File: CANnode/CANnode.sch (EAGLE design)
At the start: 244 parts, among them IC1 ISO1050DUB, IC2 ISO1050DUB, Q1 FDV302P, Q3 FDV302P, U1 LM324PW, U10 FT2232HL, U11 93LC56C-I/SN, U2 TPS70445_PWP_24, U3 LM324PW, U4 LM324PW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

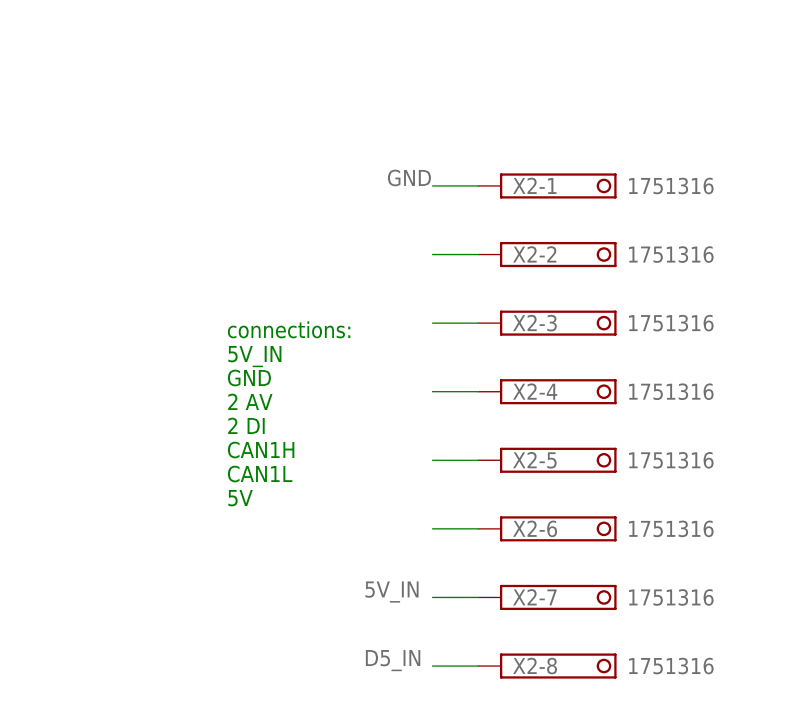
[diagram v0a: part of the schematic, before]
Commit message: Finished Debug headers
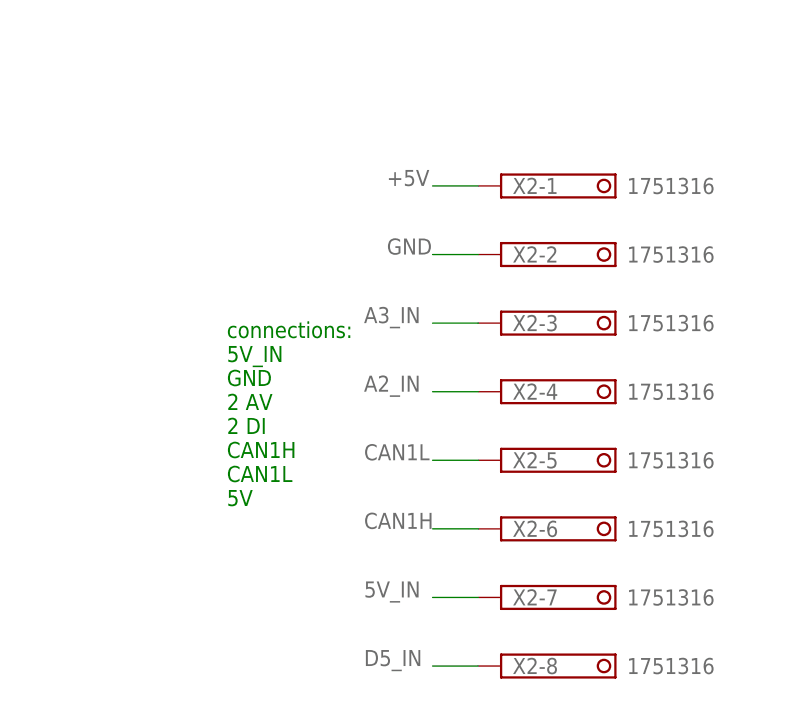
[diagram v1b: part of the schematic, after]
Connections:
- removed net N$44: X2-6.K
- removed net N$69: X2-5.K
- removed net N$70: X2-4.K
- removed net N$71: X2-3.K
- removed net N$72: X2-2.K
- net +5V: now also X2-1.K
- net A2_IN: now also X2-4.K
- net A3_IN: now also X2-3.K
- net CAN1H: now also X2-6.K
- net CAN1L: now also X2-5.K
- net GND: now also X2-2.K; no longer X2-1.K
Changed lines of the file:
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@@
 <label x="233.68" y="-160.02" size="1.778" layer="95"/>
 </segment>
+<segment>
+<pinref part="X2" gate="-6" pin="K"/>
+<wire x1="180.34" y1="-175.26" x2="175.26" y2="-175.26" width="0.1524" layer="91"/>
+<label x="167.64" y="-175.26" size="1.778" layer="95"/>
+</segment>
 </net>
 <net name="CAN1L" class="0">
@@
 <label x="233.68" y="-162.56" size="1.778" layer="95"/>
 </segment>
+<segment>
+<pinref part="X2" gate="-5" pin="K"/>
+<wire x1="180.34" y1="-167.64" x2="175.26" y2="-167.64" width="0.1524" layer="91"/>
+<label x="167.64" y="-167.64" size="1.778" layer="95"/>
+</segment>
 </net>
 <net name="CAN2L" class="0">
@@
 </segment>
 <segment>
-<pinref part="X2" gate="-1" pin="K"/>
-<wire x1="180.34" y1="-137.16" x2="175.26" y2="-137.16" width="0.1524" layer="91"/>
-<label x="170.18" y="-137.16" size="1.778" layer="95"/>
+<pinref part="X2" gate="-2" pin="K"/>
+<wire x1="180.34" y1="-144.78" x2="175.26" y2="-144.78" width="0.1524" layer="91"/>
+<label x="170.18" y="-144.78" size="1.778" layer="95"/>
 </segment>
 </net>
@@
 <wire x1="502.92" y1="-40.64" x2="505.46" y2="-40.64" width="0.1524" layer="91"/>
 </segment>
+<segment>
+<pinref part="X2" gate="-1" pin="K"/>
+<wire x1="180.34" y1="-137.16" x2="175.26" y2="-137.16" width="0.1524" layer="91"/>
+<label x="170.18" y="-137.16" size="1.778" layer="95"/>
+</segment>
 </net>
 <net name="N$45" class="0">
@@
 <wire x1="241.3" y1="-175.26" x2="248.92" y2="-175.26" width="0.1524" layer="91"/>
 </segment>
+<segment>
+<pinref part="X2" gate="-4" pin="K"/>
+<wire x1="180.34" y1="-160.02" x2="175.26" y2="-160.02" width="0.1524" layer="91"/>
+<label x="167.64" y="-160.02" size="1.778" layer="95"/>
+</segment>
 </net>
 <net name="A3_IN" class="0">
@@
 <wire x1="248.92" y1="-177.8" x2="241.3" y2="-177.8" width="0.1524" layer="91"/>
 </segment>
+<segment>
+<pinref part="X2" gate="-3" pin="K"/>
+<wire x1="180.34" y1="-152.4" x2="175.26" y2="-152.4" width="0.1524" layer="91"/>
+<label x="167.64" y="-152.4" size="1.778" layer="95"/>
+</segment>
 </net>
 <net name="A7_IN" class="0">
@@
 </segment>
 </net>
-<net name="N$44" class="0">
-<segment>
-<pinref part="X2" gate="-6" pin="K"/>
-<wire x1="180.34" y1="-175.26" x2="175.26" y2="-175.26" width="0.1524" layer="91"/>
-</segment>
-</net>
-<net name="N$69" class="0">
-<segment>
-<pinref part="X2" gate="-5" pin="K"/>
-<wire x1="180.34" y1="-167.64" x2="175.26" y2="-167.64" width="0.1524" layer="91"/>
-</segment>
-</net>
-<net name="N$70" class="0">
-<segment>
-<pinref part="X2" gate="-4" pin="K"/>
-<wire x1="180.34" y1="-160.02" x2="175.26" y2="-160.02" width="0.1524" layer="91"/>
-</segment>
-</net>
-<net name="N$71" class="0">
-<segment>
-<pinref part="X2" gate="-3" pin="K"/>
-<wire x1="180.34" y1="-152.4" x2="175.26" y2="-152.4" width="0.1524" layer="91"/>
-</segment>
-</net>
-<net name="N$72" class="0">
-<segment>
-<pinref part="X2" gate="-2" pin="K"/>
-<wire x1="180.34" y1="-144.78" x2="175.26" y2="-144.78" width="0.1524" layer="91"/>
-</segment>
-</net>

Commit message: Updated silkscreen, some ground pours, added pullup on jtag select line.
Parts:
- removed SV1: (no value), con-lsta:FE15-2
- added C75: 100nF, rcl:C-EUC0402
- added R60: 39K, resistor:R-US_R0402
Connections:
- net +3V3: now also R60.2
- net GND: now also C75.2, U2.EPAD
- net JTAG_SEL: now also C75.1, R60.1; no longer Q3.G
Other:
- note added: "to mounting holes"
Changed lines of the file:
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@@
 <setting verticaltext="up"/>
 </settings>
-<grid distance="0.1" unitdist="inch" unit="inch" style="lines" multiple="1" display="no" altdistance="0.01" altunitdist="inch" altunit="inch"/>
+<grid distance="0.01" unitdist="inch" unit="inch" style="lines" multiple="1" display="no" altdistance="0.01" altunitdist="inch" altunit="inch"/>
 <layers>
 <layer number="1" name="Top" color="4" fill="1" visible="no" active="no"/>
@@
 <part name="TP1" library="testpad" deviceset="TPS" device="B1,27"/>
 <part name="P+4" library="supply1" deviceset="+5V" device=""/>
-<part name="+3V10" library="supply1" deviceset="+3V3" device=""/>
 <part name="R61" library="rcl" deviceset="R-US_" device="R0402" value="698"/>
 <part name="C11" library="rcl" deviceset="C-EU" device="C0402" value="1uF"/>
@@
 <part name="C44" library="rcl" deviceset="C-EU" device="C0402" value=".01uF"/>
 <part name="C45" library="rcl" deviceset="C-EU" device="C0402" value=".01uF"/>
-<part name="U$2" library="supply1" deviceset="+1V2" device=""/>
 <part name="D4" library="eagle-ltspice" deviceset="R" device="R0402" value="TVS DIODE"/>
 <part name="D5" library="eagle-ltspice" deviceset="R" device="R0402" value="TVS DIODE"/>
@@
 <part name="GND123" library="supply1" deviceset="GND" device=""/>
 <part name="F1" library="adafruit" deviceset="PTCFUSE" device="-1206" value="0ZCJ0050AF2E"/>
-<part name="SV1" library="con-lsta" deviceset="FE15-2" device=""/>
 <part name="X2" library="con-phoenix-350" deviceset="1751316" device=""/>
+<part name="+1V1" library="supply1" deviceset="+3V3" device="" value="+3V3"/>
+<part name="R60" library="resistor" deviceset="R-US_" device="R0402" value="39K"/>
+<part name="C75" library="rcl" deviceset="C-EU" device="C0402" value="100nF"/>
+<part name="GND124" library="supply1" deviceset="GND" device=""/>
 </parts>
 <sheets>
@@
 <text x="548.64" y="-345.44" size="1.778" layer="91" font="fixed">16 KHz filter</text>
 <text x="492.76" y="-347.98" size="1.778" layer="91" font="fixed">16 KHz filter</text>
-<text x="251.46" y="-48.26" size="2.54" layer="91">Debug Header</text>
+<text x="177.8" y="-129.54" size="2.54" layer="91">Debug Header</text>
 <text x="248.92" y="-144.78" size="2.54" layer="91">Autosport Connector</text>
 <text x="160.02" y="-345.44" size="2.54" layer="97">XDS100V2 CPLD</text>
@@
 CAN1L
 5V</text>
+<text x="25.654" y="-144.018" size="1.778" layer="91">to mounting holes</text>
 </plain>
 <instances>
@@
 <instance part="GND8" gate="1" x="50.8" y="-5.08"/>
 <instance part="TP1" gate="G$1" x="116.84" y="-30.48"/>
-<instance part="P+4" gate="1" x="254" y="-55.88"/>
-<instance part="+3V10" gate="G$1" x="274.32" y="-55.88"/>
+<instance part="P+4" gate="1" x="175.26" y="-129.54"/>
 <instance part="R61" gate="G$1" x="599.44" y="-96.52"/>
 <instance part="C11" gate="G$1" x="589.28" y="-101.6"/>
@@
 <instance part="C44" gate="G$1" x="645.16" y="-358.14"/>
 <instance part="C45" gate="G$1" x="642.62" y="-309.88"/>
-<instance part="U$2" gate="A" x="279.4" y="-60.96"/>
 <instance part="D4" gate="G$1" x="502.92" y="-104.14" rot="R90"/>
 <instance part="D5" gate="G$1" x="553.72" y="-104.14" rot="R90"/>
@@
 <instance part="GND123" gate="1" x="58.42" y="-5.08"/>
 <instance part="F1" gate="G$1" x="15.24" y="10.16"/>
-<instance part="SV1" gate="1" x="264.16" y="-83.82"/>
 <instance part="X2" gate="-1" x="182.88" y="-137.16"/>
 <instance part="X2" gate="-2" x="182.88" y="-144.78"/>
@@
 <instance part="X2" gate="-8" x="182.88" y="-190.5"/>
 <instance part="X2" gate="-9" x="182.88" y="-198.12"/>
+<instance part="+1V1" gate="G$1" x="21.59" y="-278.892" smashed="yes">
+<attribute name="VALUE" x="17.78" y="-277.622" size="1.778" layer="96"/>
+</instance>
+<instance part="R60" gate="G$1" x="21.59" y="-290.576" rot="R90"/>
+<instance part="C75" gate="G$1" x="21.59" y="-323.596"/>
+<instance part="GND124" gate="1" x="21.59" y="-334.772"/>
 </instances>
 <busses>
@@
 </segment>
 <segment>
-<pinref part="+3V10" gate="G$1" pin="+3V3"/>
-<wire x1="274.32" y1="-58.42" x2="274.32" y2="-66.04" width="0.1524" layer="91"/>
-</segment>
-<segment>
 <pinref part="+1V20" gate="G$1" pin="+3V3"/>
 <pinref part="U9" gate="U1" pin="VCCIO2"/>
@@
 <junction x="454.66" y="48.26"/>
 </segment>
+<segment>
+<wire x1="21.59" y1="-285.496" x2="21.59" y2="-281.432" width="0.1524" layer="91"/>
+<pinref part="+1V1" gate="G$1" pin="+3V3"/>
+<pinref part="R60" gate="G$1" pin="2"/>
+</segment>
 </net>
 <net name="+1V2" class="0">
@@
 <junction x="325.12" y="63.5"/>
 </segment>
-<segment>
-<wire x1="279.4" y1="-68.58" x2="279.4" y2="-63.5" width="0.1524" layer="91"/>
-<pinref part="U$2" gate="A" pin="+1V2"/>
-</segment>
 </net>
 <net name="N$2" class="0">
@@
 </segment>
 <segment>
-<wire x1="210.82" y1="15.24" x2="200.66" y2="15.24" width="0.1524" layer="91"/>
+<wire x1="210.82" y1="15.24" x2="203.2" y2="15.24" width="0.1524" layer="91"/>
 <pinref part="U2" gate="A" pin="GND/HEATSINK"/>
+<pinref part="U2" gate="A" pin="EPAD"/>
+<wire x1="203.2" y1="15.24" x2="200.66" y2="15.24" width="0.1524" layer="91"/>
+<wire x1="200.66" y1="17.78" x2="203.2" y2="17.78" width="0.1524" layer="91"/>
+<wire x1="203.2" y1="17.78" x2="203.2" y2="15.24" width="0.1524" layer="91"/>
+<junction x="203.2" y="15.24"/>
 </segment>
 <segment>
@@
 <label x="170.18" y="-144.78" size="1.778" layer="95"/>
 </segment>
+<segment>
+<pinref part="GND124" gate="1" pin="GND"/>
+<pinref part="C75" gate="G$1" pin="2"/>
+<wire x1="21.59" y1="-332.232" x2="21.59" y2="-328.676" width="0.1524" layer="91"/>
+</segment>
 </net>
 <net name="A0_BUFFERED" class="0">
@@
 <net name="+5V" class="0">
 <segment>
-<pinref part="P+4" gate="1" pin="+5V"/>
-<wire x1="254" y1="-66.04" x2="254" y2="-58.42" width="0.1524" layer="91"/>
-</segment>
-<segment>
 <pinref part="U3" gate="A" pin="VCC"/>
 <wire x1="408.94" y1="-109.22" x2="411.48" y2="-109.22" width="0.1524" layer="91"/>
@@
 <pinref part="X2" gate="-1" pin="K"/>
 <wire x1="180.34" y1="-137.16" x2="175.26" y2="-137.16" width="0.1524" layer="91"/>
-<label x="170.18" y="-137.16" size="1.778" layer="95"/>
+<pinref part="P+4" gate="1" pin="+5V"/>
+<wire x1="175.26" y1="-137.16" x2="175.26" y2="-132.08" width="0.1524" layer="91"/>
 </segment>
 </net>
@@
 <pinref part="D35" gate="G$1" pin="2"/>
 <wire x1="662.94" y1="-353.06" x2="668.02" y2="-353.06" width="0.1524" layer="91"/>
-<wire x1="662.94" y1="-355.6" x2="662.94" y2="-358.14" width="0.1524" layer="91"/>
 <wire x1="662.94" y1="-355.6" x2="662.94" y2="-353.06" width="0.1524" layer="91"/>
 <junction x="662.94" y="-353.06"/>
@@
 <net name="JTAG_SEL" class="0">
 <segment>
-<pinref part="Q3" gate="A" pin="G"/>
-<wire x1="41.91" y1="-303.53" x2="21.59" y2="-303.53" width="0.1524" layer="91"/>
 <label x="21.59" y="-303.53" size="1.778" layer="95"/>
+<pinref part="R60" gate="G$1" pin="1"/>
+<pinref part="C75" gate="G$1" pin="1"/>
+<wire x1="21.59" y1="-321.056" x2="21.59" y2="-303.53" width="0.1524" layer="91"/>
+<wire x1="21.59" y1="-303.53" x2="21.59" y2="-295.656" width="0.1524" layer="91"/>
+<wire x1="42.164" y1="-303.53" x2="21.59" y2="-303.53" width="0.1524" layer="91"/>
+<junction x="21.59" y="-303.53"/>
 </segment>
 </net>
@@
 <pinref part="R59" gate="G$1" pin="2"/>
 <label x="60.96" y="-144.78" size="1.778" layer="95"/>
-<wire x1="-2.54" y1="-144.78" x2="25.4" y2="-144.78" width="0.1524" layer="91"/>
-<wire x1="25.4" y1="-144.78" x2="25.4" y2="-154.94" width="0.1524" layer="91"/>
-<wire x1="25.4" y1="-154.94" x2="25.4" y2="-165.1" width="0.1524" layer="91"/>
-<wire x1="25.4" y1="-165.1" x2="25.4" y2="-175.26" width="0.1524" layer="91"/>
-<wire x1="25.4" y1="-175.26" x2="-2.54" y2="-175.26" width="0.1524" layer="91"/>
-<wire x1="-2.54" y1="-165.1" x2="25.4" y2="-165.1" width="0.1524" layer="91"/>
-<junction x="25.4" y="-165.1"/>
-<wire x1="-2.54" y1="-154.94" x2="25.4" y2="-154.94" width="0.1524" layer="91"/>
-<junction x="25.4" y="-154.94"/>
 <wire x1="25.4" y1="-144.78" x2="71.12" y2="-144.78" width="0.1524" layer="91"/>
-<junction x="25.4" y="-144.78"/>
 </segment>
 </net>

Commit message: Layout changes.
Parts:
- added C76: .1uF, rcl:C-EUC0402
- added D36: (no value), zetex:DSOD323
- C7: value (none) -> .1uF
- R3: value 499k -> 250
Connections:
- net +3V3: now also C76.1
- net GND: now also C76.2
- net JTAG_SEL: now also Q3.G
- net N$12: now also D36.C
- net N$13: now also D36.A
- net SCI1_RX: now also U7.LINRX
- net SCI1_TX: now also U7.LINTX
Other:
- note removed: "GND"
- note removed: "made a test point"
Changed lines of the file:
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@@
 <setting verticaltext="up"/>
 </settings>
-<grid distance="0.01" unitdist="inch" unit="inch" style="lines" multiple="1" display="no" altdistance="0.01" altunitdist="inch" altunit="inch"/>
+<grid distance="0.1" unitdist="inch" unit="inch" style="lines" multiple="1" display="no" altdistance="0.01" altunitdist="inch" altunit="inch"/>
 <layers>
 <layer number="1" name="Top" color="4" fill="1" visible="no" active="no"/>
@@
 <part name="+3V1" library="supply1" deviceset="+3V3" device=""/>
 <part name="U$1" library="supply1" deviceset="+1V2" device=""/>
-<part name="R3" library="resistor" deviceset="R-US_" device="R0402" value="499k"/>
+<part name="R3" library="resistor" deviceset="R-US_" device="R0402" value="250"/>
 <part name="LED1" library="led" deviceset="LED" device=""/>
 <part name="R4" library="varistor" deviceset="VARISTOR" device="CN0805"/>
@@
 <part name="P+1" library="supply1" deviceset="+5V" device=""/>
 <part name="P+2" library="supply1" deviceset="+5V" device=""/>
-<part name="D1" library="docu-dummy" deviceset="DIODE" device=""/>
 <part name="R7" library="resistor" deviceset="R-US_" device="R0402" value="100k"/>
 <part name="+3V2" library="supply1" deviceset="+3V3" device=""/>
@@
 <part name="IC1" library="texas" deviceset="ISO1050" device="DUB"/>
 <part name="IC2" library="texas" deviceset="ISO1050" device="DUB"/>
-<part name="C7" library="rcl" deviceset="C-EU" device="C0402"/>
+<part name="C7" library="rcl" deviceset="C-EU" device="C0402" value=".1uF"/>
 <part name="+3V4" library="supply1" deviceset="+3V3" device=""/>
 <part name="+3V5" library="supply1" deviceset="+3V3" device=""/>
@@
 <part name="C75" library="rcl" deviceset="C-EU" device="C0402" value="100nF"/>
 <part name="GND124" library="supply1" deviceset="GND" device=""/>
+<part name="C76" library="rcl" deviceset="C-EU" device="C0402" value=".1uF"/>
+<part name="GND125" library="supply1" deviceset="GND" device=""/>
+<part name="GND126" library="supply1" deviceset="GND" device=""/>
+<part name="GND127" library="supply1" deviceset="GND" device=""/>
+<part name="GND128" library="supply1" deviceset="GND" device=""/>
+<part name="GND129" library="supply1" deviceset="GND" device=""/>
+<part name="GND130" library="supply1" deviceset="GND" device=""/>
+<part name="D36" library="zetex" deviceset="D" device="SOD323"/>
 </parts>
 <sheets>
 <sheet>
 <plain>
-<text x="93.98" y="17.78" size="1.27" layer="91">GND</text>
-<text x="93.98" y="-2.54" size="1.27" layer="91">GND</text>
-<text x="93.98" y="-10.16" size="1.27" layer="91">GND</text>
-<text x="208.28" y="15.24" size="1.27" layer="91">GND</text>
-<text x="208.28" y="-12.7" size="1.27" layer="91">GND</text>
 <text x="104.14" y="48.26" size="5.08" layer="91">Dual Channel Power Supply (LDO)</text>
 <text x="472.44" y="81.28" size="5.08" layer="91">Transceivers</text>
@@
 <text x="304.8" y="73.66" size="1.778" layer="91">???? What about this extra pin? and where
  is VCC_SRAM, and VNMA?</text>
-<text x="71.12" y="-38.1" size="1.778" layer="91">made a test point</text>
 <text x="22.86" y="-73.66" size="1.778" layer="91">move TVS to after resistor to limit current</text>
 <text x="20.32" y="-109.22" size="3.81" layer="91">THESE ARE PLACEHOLDER RESISTERS THAT WE WILL
@@
 <instance part="P+1" gate="1" x="513.08" y="55.88" rot="MR0"/>
 <instance part="P+2" gate="1" x="497.84" y="-15.24"/>
-<instance part="D1" gate="G$1" x="78.74" y="-33.02" rot="R180"/>
 <instance part="R7" gate="G$1" x="68.58" y="-25.4" rot="R90"/>
 <instance part="+3V2" gate="G$1" x="68.58" y="-15.24"/>
@@
 <instance part="C7" gate="G$1" x="482.6" y="-25.4"/>
 <instance part="+3V4" gate="G$1" x="477.52" y="-17.78"/>
-<instance part="+3V5" gate="G$1" x="477.52" y="45.72"/>
+<instance part="+3V5" gate="G$1" x="477.52" y="55.88"/>
 <instance part="GND43" gate="1" x="2.54" y="-101.6"/>
 <instance part="GND44" gate="1" x="12.7" y="-111.76"/>
@@
 <instance part="C75" gate="G$1" x="21.59" y="-323.596"/>
 <instance part="GND124" gate="1" x="21.59" y="-334.772"/>
+<instance part="C76" gate="G$1" x="482.6" y="48.26"/>
+<instance part="GND125" gate="1" x="482.6" y="40.64"/>
+<instance part="GND126" gate="1" x="210.82" y="-15.24"/>
+<instance part="GND127" gate="1" x="93.98" y="-12.7"/>
+<instance part="GND128" gate="1" x="93.98" y="-5.08"/>
+<instance part="GND129" gate="1" x="210.82" y="7.62"/>
+<instance part="GND130" gate="1" x="93.98" y="15.24"/>
+<instance part="D36" gate="G$1" x="78.74" y="-33.02" rot="R180"/>
 </instances>
 <busses>
@@
 <segment>
 <pinref part="+3V5" gate="G$1" pin="+3V3"/>
-<wire x1="477.52" y1="43.18" x2="477.52" y2="33.02" width="0.1524" layer="91"/>
+<wire x1="477.52" y1="53.34" x2="477.52" y2="50.8" width="0.1524" layer="91"/>
+<wire x1="477.52" y1="50.8" x2="477.52" y2="33.02" width="0.1524" layer="91"/>
 <wire x1="477.52" y1="33.02" x2="480.06" y2="33.02" width="0.1524" layer="91"/>
 <pinref part="IC1" gate="G$1" pin="VCC1"/>
+<pinref part="C76" gate="G$1" pin="1"/>
+<wire x1="482.6" y1="50.8" x2="477.52" y2="50.8" width="0.1524" layer="91"/>
+<junction x="477.52" y="50.8"/>
 </segment>
 <segment>
@@
 <wire x1="68.58" y1="-33.02" x2="68.58" y2="-30.48" width="0.1524" layer="91"/>
 <junction x="68.58" y="-33.02"/>
+<pinref part="D36" gate="G$1" pin="C"/>
 </segment>
 </net>
@@
 <pinref part="TP1" gate="G$1" pin="PP"/>
 <label x="96.52" y="-30.48" size="1.778" layer="95"/>
+<pinref part="D36" gate="G$1" pin="A"/>
 </segment>
 </net>
@@
 <pinref part="U2" gate="A" pin="GND/HEATSINK_2"/>
 <wire x1="104.14" y1="17.78" x2="93.98" y2="17.78" width="0.1524" layer="91"/>
+<pinref part="GND130" gate="1" pin="GND"/>
 </segment>
 <segment>
@@
 <wire x1="203.2" y1="17.78" x2="203.2" y2="15.24" width="0.1524" layer="91"/>
 <junction x="203.2" y="15.24"/>
+<pinref part="GND129" gate="1" pin="GND"/>
+<wire x1="210.82" y1="10.16" x2="210.82" y2="15.24" width="0.1524" layer="91"/>
 </segment>
 <segment>
@@
 <junction x="93.98" y="5.08"/>
 <junction x="93.98" y="-2.54"/>
+<pinref part="GND128" gate="1" pin="GND"/>
 </segment>
 <segment>
 <wire x1="104.14" y1="-10.16" x2="93.98" y2="-10.16" width="0.1524" layer="91"/>
 <pinref part="U2" gate="A" pin="GND/HEATSINK_4"/>
+<pinref part="GND127" gate="1" pin="GND"/>
 </segment>
 <segment>
 <wire x1="210.82" y1="-12.7" x2="200.66" y2="-12.7" width="0.1524" layer="91"/>
 <pinref part="U2" gate="A" pin="GND/HEATSINK_5"/>
+<pinref part="GND126" gate="1" pin="GND"/>
 </segment>
 <segment>
@@
 <wire x1="21.59" y1="-332.232" x2="21.59" y2="-328.676" width="0.1524" layer="91"/>
 </segment>
+<segment>
+<pinref part="C76" gate="G$1" pin="2"/>
+<pinref part="GND125" gate="1" pin="GND"/>
+</segment>
 </net>
 <net name="A0_BUFFERED" class="0">
@@
 <wire x1="21.59" y1="-321.056" x2="21.59" y2="-303.53" width="0.1524" layer="91"/>
 <wire x1="21.59" y1="-303.53" x2="21.59" y2="-295.656" width="0.1524" layer="91"/>
-<wire x1="42.164" y1="-303.53" x2="21.59" y2="-303.53" width="0.1524" layer="91"/>
+<wire x1="41.91" y1="-303.53" x2="21.59" y2="-303.53" width="0.1524" layer="91"/>
 <junction x="21.59" y="-303.53"/>
+<pinref part="Q3" gate="A" pin="G"/>
 </segment>
 </net>
@@
 <pinref part="R103" gate="G$1" pin="2"/>
 </segment>
+<segment>
+<pinref part="U7" gate="A" pin="LINRX"/>
+<wire x1="431.8" y1="-66.04" x2="442.722" y2="-66.04" width="0.1524" layer="91"/>
+<label x="433.324" y="-66.04" size="1.778" layer="95"/>
+</segment>
 </net>
 <net name="SCI1_TX" class="0">
@@
 <pinref part="R104" gate="G$1" pin="2"/>
 </segment>
+<segment>
+<pinref part="U7" gate="A" pin="LINTX"/>
+<wire x1="431.8" y1="-63.5" x2="442.722" y2="-63.5" width="0.1524" layer="91"/>
+<label x="433.324" y="-63.5" size="1.778" layer="95"/>
+</segment>
 </net>
